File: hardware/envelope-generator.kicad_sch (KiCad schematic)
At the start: 95 parts, among them J1 Power bus, J10 EG 1 Out, J2 SWD, J3 Serial Dongle, J4 EG 2 Out, J5 Gate 1 In, J6 CAN, J7 Gate 2 In, SW1 Gate Src, SW2 EG Modes, SW3 NRST, U1 TL072, U2 MC34063AD, U3 TL072, U4 LM4040DBZ-3, U8 STM32C092KCT6, U9 TCAN3413, Y1 48 MHz

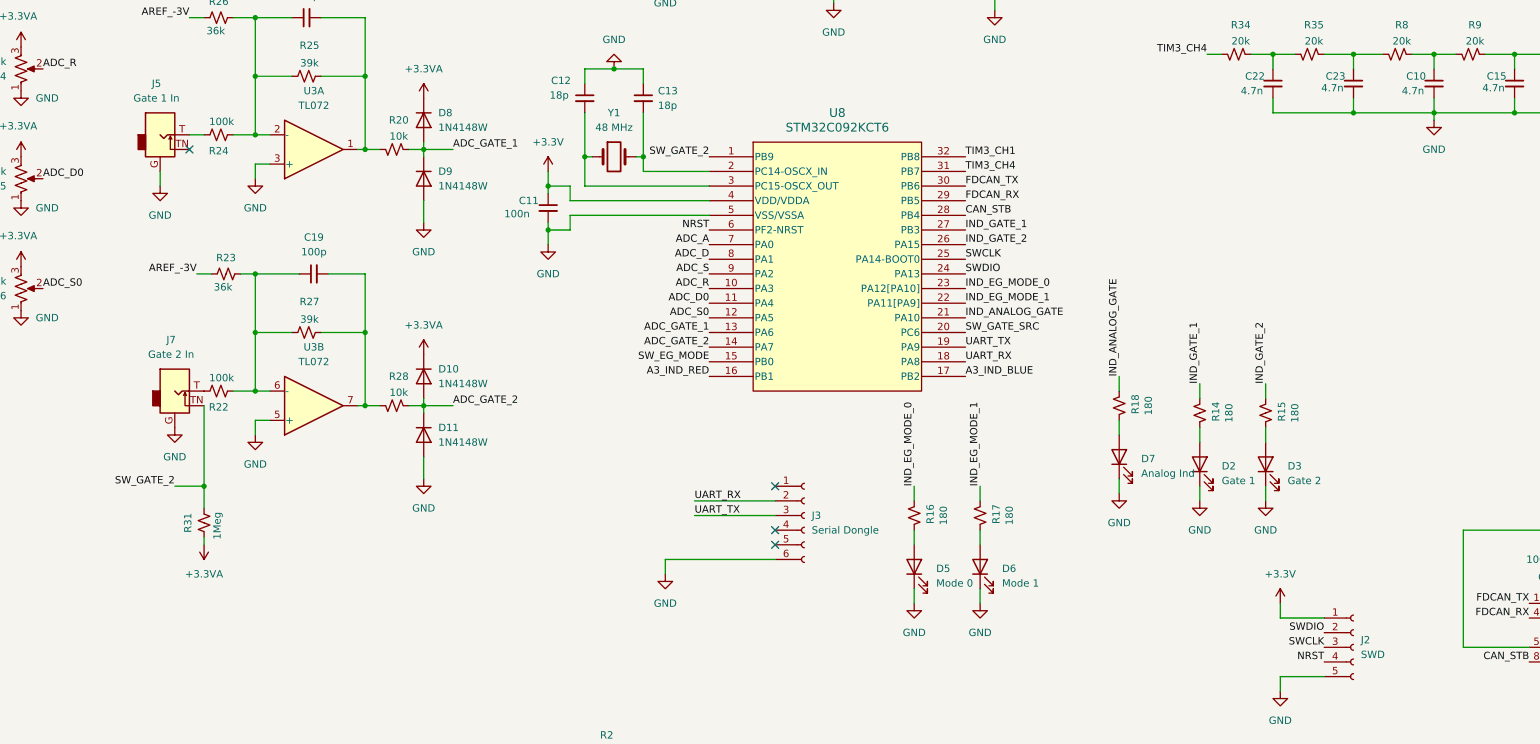
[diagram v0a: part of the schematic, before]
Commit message: Extend maximum number of EG modes to 8
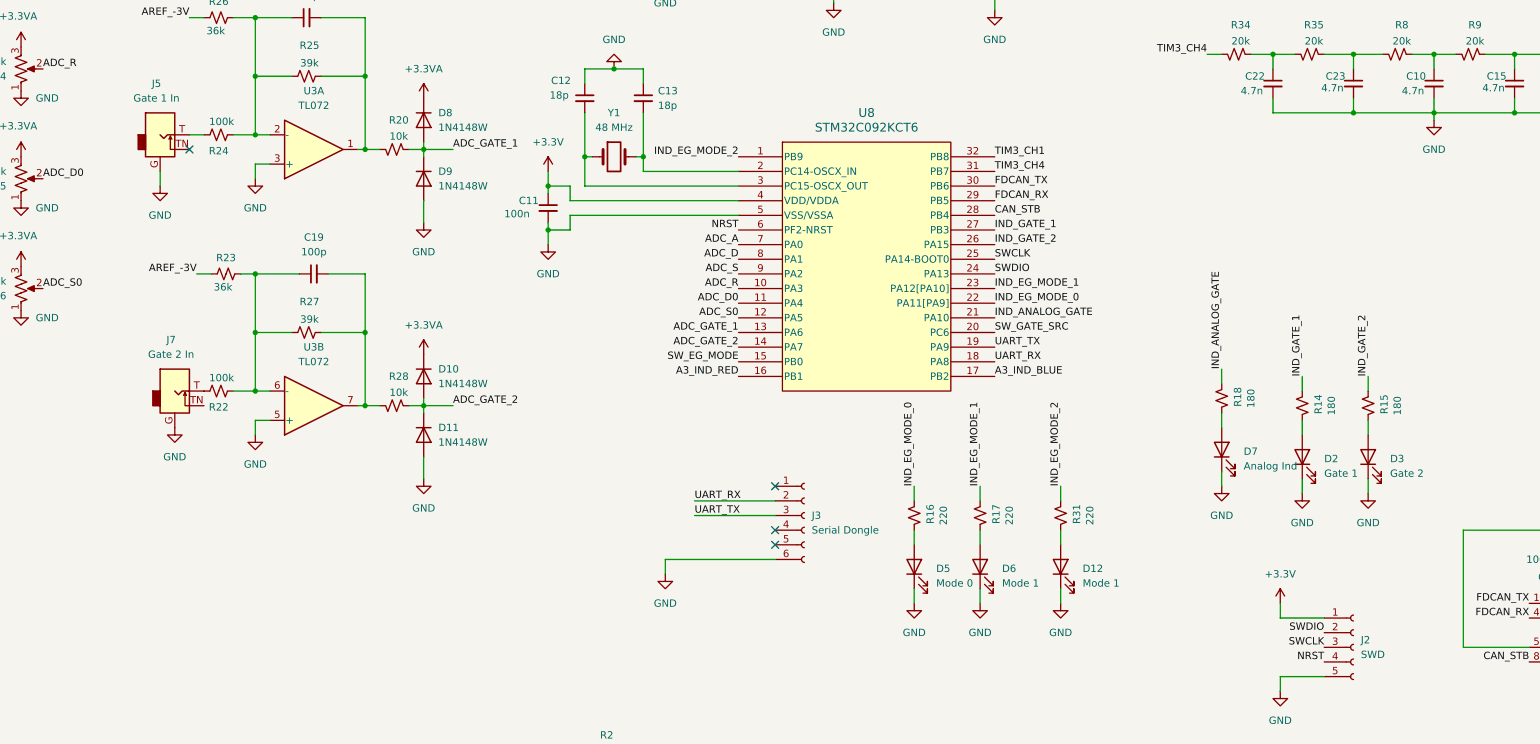
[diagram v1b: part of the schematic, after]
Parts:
- added D12: Mode 1, LED_THT:LED_D3.0mm, symbol Device:LED
- R16, R17: value 180 -> 220
- R31: value 1Meg -> 220; footprint Resistor_SMD:R_0805_2012Metric_Pad1.20x1.40mm_HandSolder -> Resistor_SMD:R_0603_1608Metric
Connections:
- net +3.3VA: no longer R31.1
- net GND: now also D12.1 (K)
- net IND_EG_MODE_0: now also U8.22 (PA11[PA9]); no longer U8.23 (PA12[PA10])
- net IND_EG_MODE_1: now also U8.23 (PA12[PA10]); no longer U8.22 (PA11[PA9])
- removed net SW_GATE_2: J7.TN, R31.2, U8.1 (PB9)
- new net: D12.2 (A), R31.2
- new net IND_EG_MODE_2: R31.1, U8.1 (PB9)
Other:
- moved on the sheet: D2, D3, D7, R14, R15, R18, U8

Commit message: PCB design the first iteration
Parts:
- removed C21, C22, C23: 4.7n, Capacitor_SMD:C_0603_1608Metric, symbol Device:C_Small
- removed C9: 47u, Capacitor_THT:CP_Radial_D5.0mm_P2.50mm, symbol Device:C_Polarized_Small
- removed D10, D11, D8, D9: 1N4148W, Diode_THT:D_DO-35_SOD27_P7.62mm_Horizontal, symbol Diode:1N4148W
- removed D12, D6: Mode 1, LED_THT:LED_D3.0mm, symbol Device:LED
- removed D5: Mode 0, LED_THT:LED_D3.0mm, symbol Device:LED
- removed J2: SWD, Connector_PinSocket_2.54mm:PinSocket_1x05_P2.54mm_Vertical, symbol Connector:Conn_01x05_Socket
- removed J3: Serial Dongle, Connector_PinSocket_2.54mm:PinSocket_1x06_P2.54mm_Vertical, symbol Connector:Conn_01x06_Socket
- removed L2: 150u, Inductor_SMD:L_1008_2520Metric, symbol Device:L_Small
- removed SW2: EG Modes, Tactile_Switches:SW4_1825910-B_TEC, symbol TactileSwitches:Tactile_Switch
- removed U3: TL072, Package_DIP:DIP-8_W7.62mm, symbol Amplifier_Operational1:TL072
- removed U8: STM32C092KCT6, stm32c092kct6:LQFP-32_STM-M, symbol stm32c092kct6:STM32C092KCT6
- removed Y1: 48 MHz, Crystal:Crystal_HC49-4H_Vertical, symbol Device:Crystal
- added Brd1: SSD1306, SSD1306:128x64OLED_aki, symbol SSD1306-128x64_OLED:SSD1306
- added C9: 10u, Capacitor_SMD:C_0603_1608Metric, symbol Device:C_Small
- added D10: Analog SRC 2, Synth:LED_D3.0mm, symbol Device:LED
- added D5: 1N4148WS, Diode_SMD:D_SOD-323, symbol Diode:1N4148WS
- added J2: Dual or Voice 1 Out, Synth:Thonkiconn_Stereo, symbol Synth:AudioJack2_Ground
- added J3: Conn_01x03_Socket, Connector_PinSocket_1.27mm:PinSocket_1x03_P1.27mm_Vertical, symbol Connector:Conn_01x03_Socket
- added J8: SWD, Connector_Synth:CONN_2x10_3220-10-0100-00_CNC, symbol Connector_Generic:Conn_02x05_Odd_Even
- added J9: CV 1 In, Synth:Thonkiconn, symbol Synth:AudioJack_Ground_Switch
- added R36: 36k, Resistor_SMD:R_0603_1608Metric_Pad0.98x0.95mm_HandSolder, symbol Device:R_Small_US
- added R37: 18k, Resistor_SMD:R_0603_1608Metric_Pad0.98x0.95mm_HandSolder, symbol Device:R_Small_US
- added RV7, RV8: 10k, Synth:ALPHA_9MM, symbol Synth:R_Potentiometer_US
- added U10: CD4051B, Package_SO:TSSOP-16_4.4x5mm_P0.65mm, symbol Analog_Switch:CD4051B
- added U3: MCP6004, Package_SO:SOIC-14_3.9x8.7mm_P1.27mm, symbol Amplifier_Operational:MCP6004
- added U5: STM32G0B1CBTx, Package_QFP:LQFP-48_7x7mm_P0.5mm, symbol MCU_ST_STM32G0:STM32G0B1CBTx
- added U6: PEL12D-4225S-S2024, PEL12D:TO_4225S-S2024, symbol PEL12D:PEL12D-4225S-S2024
- added U7: LM4040DBZ-3, Package_TO_SOT_SMD:SOT-23, symbol Reference_Voltage:LM4040DBZ-3
- added U8: LM393, Package_SO:SOIC-8_3.9x4.9mm_P1.27mm, symbol Comparator:LM393
- added Y1: 16MHz, Crystal:Crystal_SMD_Abracon_ABM8G-4Pin_3.2x2.5mm, symbol Device:Crystal_GND24_Small
- C1, C2, C6: footprint Capacitor_THT:CP_Radial_D5.0mm_P2.50mm -> Capacitor_SMD:CP_Elec_6.3x5.4_Nichicon
- C10, C15: footprint Capacitor_SMD:C_0603_1608Metric -> Capacitor_SMD:C_0603_1608Metric_Pad1.08x0.95mm_HandSolder
- C17: value 100n -> 2.2u; footprint Capacitor_SMD:C_0603_1608Metric -> Capacitor_SMD:C_0603_1608Metric_Pad1.08x0.95mm_HandSolder
- C18, C19: value 100p -> 1n
- C20: value 4.7n -> 100n; footprint Capacitor_SMD:C_0603_1608Metric -> Capacitor_SMD:C_0603_1608Metric_Pad1.08x0.95mm_HandSolder
- C7: value 4.7n -> 100n
- C8: value 4.7n -> 1u; footprint Capacitor_SMD:C_0603_1608Metric -> Capacitor_SMD:C_0603_1608Metric_Pad1.08x0.95mm_HandSolder
- D2, D3: footprint LED_THT:LED_D3.0mm -> Synth:LED_D3.0mm
- D7: value Analog Ind -> Analog SRC 1; footprint LED_THT:LED_D3.0mm -> Synth:LED_D3.0mm
- J1: footprint Synth:CONN10_302-S101_OST -> Connector_IDC:IDC-Header_2x05_P2.54mm_Vertical
- J10: value EG 1 Out -> CV 2 In
- R10, R6: value 20k -> 10k
- R16, R17: value 220 -> 680
- R19, R21, R24, R26: footprint Resistor_SMD:R_0805_2012Metric_Pad1.20x1.40mm_HandSolder -> Resistor_SMD:R_0603_1608Metric_Pad0.98x0.95mm_HandSolder
- R20: footprint Resistor_SMD:R_0603_1608Metric -> Resistor_SMD:R_0603_1608Metric_Pad0.98x0.95mm_HandSolder
- R22: value 100k -> 470k; footprint Resistor_SMD:R_0805_2012Metric_Pad1.20x1.40mm_HandSolder -> Resistor_SMD:R_0603_1608Metric_Pad0.98x0.95mm_HandSolder
- R23: value 36k -> 470k; footprint Resistor_SMD:R_0805_2012Metric_Pad1.20x1.40mm_HandSolder -> Resistor_SMD:R_0603_1608Metric_Pad0.98x0.95mm_HandSolder
- R25: value 39k -> 36k; footprint Resistor_SMD:R_0805_2012Metric_Pad1.20x1.40mm_HandSolder -> Resistor_SMD:R_0603_1608Metric_Pad0.98x0.95mm_HandSolder
- R27: value 39k -> 180; footprint Resistor_SMD:R_0805_2012Metric_Pad1.20x1.40mm_HandSolder -> Resistor_SMD:R_0603_1608Metric
- R28: value 10k -> 100k; footprint Resistor_SMD:R_0603_1608Metric -> Resistor_SMD:R_0603_1608Metric_Pad0.98x0.95mm_HandSolder
- R31: value 220 -> 3.3k; footprint Resistor_SMD:R_0603_1608Metric -> Resistor_SMD:R_0603_1608Metric_Pad0.98x0.95mm_HandSolder
- R32: value 20k -> 15k; footprint Resistor_SMD:R_0603_1608Metric -> Resistor_SMD:R_0603_1608Metric_Pad0.98x0.95mm_HandSolder
- R33, R9: value 20k -> 100k; footprint Resistor_SMD:R_0603_1608Metric -> Resistor_SMD:R_0603_1608Metric_Pad0.98x0.95mm_HandSolder
- R34, R5, R8: value 20k -> 36k; footprint Resistor_SMD:R_0603_1608Metric -> Resistor_SMD:R_0603_1608Metric_Pad0.98x0.95mm_HandSolder
- R35: value 20k -> 18k; footprint Resistor_SMD:R_0603_1608Metric -> Resistor_SMD:R_0603_1608Metric_Pad0.98x0.95mm_HandSolder
- R4: value 20k -> 10k; footprint Resistor_SMD:R_0603_1608Metric -> Resistor_SMD:R_0603_1608Metric_Pad0.98x0.95mm_HandSolder
- SW1: value Gate Src -> USER_SW
- SW3: value NRST -> USER_SW
- U1: footprint Package_DIP:DIP-8_W7.62mm -> Package_SO:TSSOP-8_3x3mm_P0.65mm
- U4: value LM4040DBZ-3 -> LM4040DBZ-10
- U9: footprint Package_TO_SOT_SMD:TSOT-23-8_HandSoldering -> Package_TO_SOT_SMD:TSOT-23-8
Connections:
- net +3.3VA is gone; now on net AREF_3V: RV1.3, RV2.3, RV3.3, RV4.3, RV5.3, RV6.3
- net SW_GATE_SRC is gone; now on net NRST: SW1.3, SW1.4
- net TIM3_CH1 is gone; now on net GATE_REF: R32.2
- net TIM3_CH4 is gone; now on an unnamed net: R34.2
- net +12V: now also C7.1, R4.2, U8.8 (V+); no longer C16.1
- net +3.3V: now also C16.1, C17.1, C20.1, R22.2, R23.2, Brd1.2 (VCC), C9.1, D5.1 (K), J8.1 (Pin_1), U10.16 (VDD), U3.4 (V+), U5.4 (VBAT), U5.6 (VDD)
- net -12V: no longer C17.2
- net A3_IND_BLUE: now also U5.23 (PB11)
- net A3_IND_RED: now also U5.24 (PB12)
- net ADC_GATE_1: now also C18.2, R25.1, U3.8, U5.14 (PA3), U8.3 (+); no longer R20.1
- net ADC_GATE_2: now also C19.2, R5.1, U3.14, U5.13 (PA2), U8.5 (+); no longer R28.1
- net AREF_-3V: now also R34.1, R8.1, R36.1; no longer R23.1
- net CAN_STB: now also U5.1 (PC13)
- net EG_1_OUT: now also J2.S; no longer J10.T
- net FDCAN_RX: now also U5.47 (PB8)
- net FDCAN_TX: now also U5.48 (PB9)
- net GND: now also C17.2, R20.1, R32.1, RV1.MP, RV2.MP, RV3.MP, RV4.MP, RV5.MP, RV6.MP, Brd1.1 (GND), D10.1 (K), J2.G, J3.3 (Pin_3), J8.3 (Pin_3), J8.5 (Pin_5), J8.9 (Pin_9), J9.G, RV7.1, RV7.MP, RV8.1, RV8.MP, U10.6 (INH), U10.7 (VEE), U10.8 (VSS), U3.10 (+), U3.11 (V-), U3.12 (+), U3.3 (+), U3.5 (+), U5.7 (VSS), U6.1, U6.C, U7.2 (A), U8.4 (V-), Y1.2 (G), Y1.4 (G); no longer C10.2, C15.2, C17.1
- net IND_GATE_1: now also U5.40 (PD2)
- net IND_GATE_2: now also U5.41 (PD3)
- net NRST: now also C9.2, D5.2 (A), J8.10 (Pin_10), U5.10 (PF2); no longer SW3.3, SW3.4
- net SWCLK: now also R20.2, J8.4 (Pin_4), U5.36 (PA14)
- net SWDIO: now also J8.2 (Pin_2), U5.35 (PA13)
- net UART_RX: now also J3.1 (Pin_1), U5.46 (PB7)
- net UART_TX: now also J3.2 (Pin_2), U5.45 (PB6)
- net AREF_3V: now reaches R31.2
- net AREF_3V: now also R4.1, RV7.3, RV8.3, U5.5 (VREF+), U7.1 (K)
- net at R16.2: now also U6.2
- net at R35.2: now also C10.1, R33.1, U3.2 (-); no longer R34.1
- net ENCODER_IND_RED: now reaches R17.2
- net ENCODER_IND_RED: now also U5.34 (PA10/PA12)
- net OSC_IN: now reaches C13.2
- net OSC_IN: now also U5.8 (PF0), Y1.3
- net at C18.1, R24.1, R25.2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: now also U3.9 (-)
- net at R8.2: now also C19.1, R5.2, R9.1, U3.13 (-); no longer R35.1
- net OSC_OUT: now reaches C12.2
- net OSC_OUT: now also U5.9 (PF1), Y1.1
- net at J7.T: now also R9.2; no longer R22.2
- net GATE_SRC_SW_2: now reaches J7.TN
- net GATE_SRC_SW_2: now also R22.1, U5.29 (PA9/UCPD1_DBCC1)
- net at J4.TN: now also J2.T
- net GATE_SRC_SW_1: now reaches J5.TN
- net GATE_SRC_SW_1: now also R23.1, U5.28 (PA8)
- net ADC_A renamed A
- net A: now also U10.13 (X0)
- net ADC_D renamed D
- net D: now also U10.14 (X1)
- net ADC_D0 renamed D0
- net D0: now also U10.1 (X4)
- net ADC_R renamed R
- net R: now also U10.12 (X3)
- net ADC_S renamed S
- net S: now also U10.15 (X2)
- net ADC_S0 renamed S0
- net S0: now also U10.5 (X5)
- net IND_ANALOG_GATE renamed IND_ANALOG_GATE_1
- net IND_ANALOG_GATE_1: now also U5.38 (PD0)
- net IND_EG_MODE_0 renamed ENCODER_IND_GREEN
- net ENCODER_IND_GREEN: now also U5.33 (PA9/PA11)
- net IND_EG_MODE_1: no longer names the net of R17.1
- net IND_EG_MODE_1: now also U6.3
- net IND_EG_MODE_2 renamed GATE_REF
- net GATE_REF: now also C8.1, U8.2 (-), U8.6 (-)
- new net: J10.T, R28.2
- new net: J9.T, R33.2
- new net: C15.1, R28.1, R36.2, R37.2, U3.6 (-)
- new net: D10.2 (A), R27.2
- new net ADC_CV_1: C10.2, R35.1, U3.1, U5.11 (PA0)
- new net ADC_CV_2: C15.2, R37.1, U3.7, U5.12 (PA1)
- new net ADC_POTS: U10.3 (X), U5.17 (PA6)
- new net CV_ATT_1: RV7.2, U10.2 (X6)
- new net CV_ATT_2: RV8.2, U10.4 (X7)
- new net DAC_OUT_1: U1.3 (+), U5.15 (PA4)
- new net DAC_OUT_2: U1.5 (+), U5.16 (PA5)
- new net ENCODER_A: U5.30 (PC6), U6.A
- new net ENCODER_B: U5.31 (PC7), U6.B
- new net ENCODER_SW: U5.32 (PA10/UCPD1_DBCC2), U6.4
- new net GATE_TRIGGER_1: U5.42 (PB3), U8.1
- new net GATE_TRIGGER_2: U5.43 (PB4), U8.7
- new net I2C2_SDA: Brd1.4 (SDA), U5.26 (PB14)
- new net I2C_SCL: Brd1.3 (SCL), U5.25 (PB13)
- new net IND_ANALOG_GATE_2: R27.1, U5.39 (PD1)
- new net MUX_ADDR_0: U10.11 (A), U5.18 (PA7)
- new net MUX_ADDR_1: U10.10 (B), U5.19 (PB0)
- new net MUX_ADDR_2: U10.9 (C), U5.20 (PB1)
- new net USER_SW: SW3.3, SW3.4, U5.37 (PA15)
- no-connect marks 6 -> 11
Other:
- moved on the sheet: C11, C12, C13, C14, C16, C18, C19, C3, C4, C5, C6, D1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

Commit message: humps rev 0
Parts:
- added C21, C22: 470p, Capacitor_SMD:C_0603_1608Metric_Pad1.08x0.95mm_HandSolder, symbol Device:C_Small
- added D6: WP115VEGW, Synth:LED-3.0mm-3, symbol Device:LED_Dual_AKA
- added R38, R39: 180, Resistor_SMD:R_0603_1608Metric_Pad0.98x0.95mm_HandSolder, symbol Device:R_Small_US
- C12, C13: value 18p -> 9p
- C9: footprint Capacitor_SMD:C_0603_1608Metric -> Capacitor_SMD:C_0805_2012Metric
- R16, R17: value 680 -> 330
- R4: value 10k -> 2.7k
- SW1: value USER_SW -> RESET_SW; footprint Tactile_Switches:SW4_1825910-B_TEC -> Tactile_Switches:Panasonic_EVQ_Q2
- U1: footprint Package_SO:TSSOP-8_3x3mm_P0.65mm -> Package_TO_SOT_SMD:SOT-23-8
- U4: value LM4040DBZ-10 -> LM4040DBZ-3.0
- U5: value STM32G0B1CBTx -> STM32G0B1CET6
- U7: value LM4040DBZ-3 -> LM4040DBZ-3.0
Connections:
- net +3.3V: no longer C9.1
- net A3_IND_BLUE: now also U5.2 (PC14); no longer U5.23 (PB11)
- net A3_IND_RED: now also U5.3 (PC15); no longer U5.24 (PB12)
- net EG_1_OUT: now also J2.T; no longer J2.S
- net GATE_TRIGGER_1: now also U5.21 (PB2); no longer U5.42 (PB3)
- net GATE_TRIGGER_2: now also U5.22 (PB10); no longer U5.43 (PB4)
- net GND: now also C9.2, D6.2 (K)
- net NRST: now also C9.1; no longer C9.2
- net UART_RX: now also J3.2 (Pin_2); no longer J3.1 (Pin_1)
- net UART_TX: now also J3.1 (Pin_1); no longer J3.2 (Pin_2)
- net at J4.TN: now also J2.S; no longer J2.T
- net at R11.1, R13.2, U1.7: now also C22.1
- net at R10.1, R11.2, U1.6 (-): now also C22.2
- net at R6.1, R7.2, U1.2 (-): now also C21.2
- net at R1.2, R7.1, U1.1: now also C21.1
- new net: D6.1 (A1), R38.2
- new net: D6.3 (A2), R39.2
- new net PATCH_IND_GREEN: R39.1, U5.23 (PB11)
- new net PATCH_IND_RED: R38.1, U5.24 (PB12)
- no-connect marks 11 -> 7
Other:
- note added: "Patch Indicator"
- title: Analog3 Envelope Generator -> Humps D
- moved on the sheet: C9, D5
